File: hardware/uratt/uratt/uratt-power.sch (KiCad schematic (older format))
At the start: 66 parts

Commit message: uRATT rough footprint assignment and placement for fitment
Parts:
- removed A?: Pololu_Breakout_A4988, Module:Pololu_Breakout-16_15.2x20.3mm, symbol Driver_Motor:Pololu_Breakout_A4988
- removed C?: 47uF, symbol Device:CP1_Small
- removed C? (x2): 0.1uF, symbol Device:C_Small
- removed J?: Conn_01x04, symbol Connector_Generic:Conn_01x04
- removed R? (x3): 0, symbol Device:R_Small_US
- C17, C20, C23, C32: renamed from C?; footprint (none) -> Capacitor_SMD:C_0805_2012Metric
- C18, C19, C21, C22, C24, C25, C26, C27, C29, C31: renamed from C?; footprint (none) -> Capacitor_SMD:C_0603_1608Metric
- C28: renamed from C?; footprint (none) -> Capacitor_SMD:CP_Elec_5x3
- D11, D7, D8, D9: renamed from D?; footprint (none) -> LED_SMD:LED_0603_1608Metric_Pad1.05x0.95mm_HandSolder
- J6, J7, J8: renamed from J?; footprint (none) -> Connector_JST:JST_PH_B2B-PH-K_1x02_P2.00mm_Vertical
- L1: renamed from L?; footprint (none) -> Inductor_SMD:L_12x12mm_H4.5mm
- R28, R29, R30, R31, R32, R33, R34, R35, R36, R37, R38, R39, R40, R41, R42, R43, R44, R45, R46, R47, R48, R49: renamed from R?; footprint (none) -> Resistor_SMD:R_0603_1608Metric
- TP1, TP2, TP3, TP4, TP5, TP6: renamed from TP?; footprint (none) -> TestPoint:TestPoint_Pad_1.5x1.5mm
- U5: renamed from U?; footprint (none) -> Package_SO:TSSOP-8_4.4x3mm_P0.65mm
- U6: renamed from U?; footprint (none) -> Package_SO:TSSOP-16-1EP_4.4x5mm_P0.65mm
- gave numbers to parts that had none: 5
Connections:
- wire segments 250 -> 211
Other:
- note removed: "STEPPER MOTOR\nDRIVER (OPTIONAL)"

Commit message: WIP routing
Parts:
- added H1, H2, H3, H4: MountingHole, MountingHole:MountingHole_2.7mm_M2.5, symbol Mechanical:MountingHole
- C28: footprint Capacitor_SMD:CP_Elec_5x3 -> Capacitor_Tantalum_SMD:CP_EIA-6032-20_AVX-F
- GT1: renamed from R43; footprint Resistor_SMD:R_0603_1608Metric -> uratt:GND_TIE
- TP1, TP2, TP3, TP4, TP5, TP6: footprint TestPoint:TestPoint_Pad_1.5x1.5mm -> TestPoint:TestPoint_Pad_D1.0mm
- U6: footprint Package_SO:TSSOP-16-1EP_4.4x5mm_P0.65mm -> uratt:PWP0016C
- renumbered C31 to C30, C32 to C31, R28 to JP1, R29 to JP2, R30 to JP3, R31 to JP4, R32 to R26, R33 to R27, R34 to R28, R35 to R29, R36 to R30, R37 to R31, R38 to R32, R39 to R33, R40 to R34, R41 to R35, R42 to R36, R44 to R37, R45 to R38, R46 to R39, R47 to R40, R48 to R41, R49 to R42

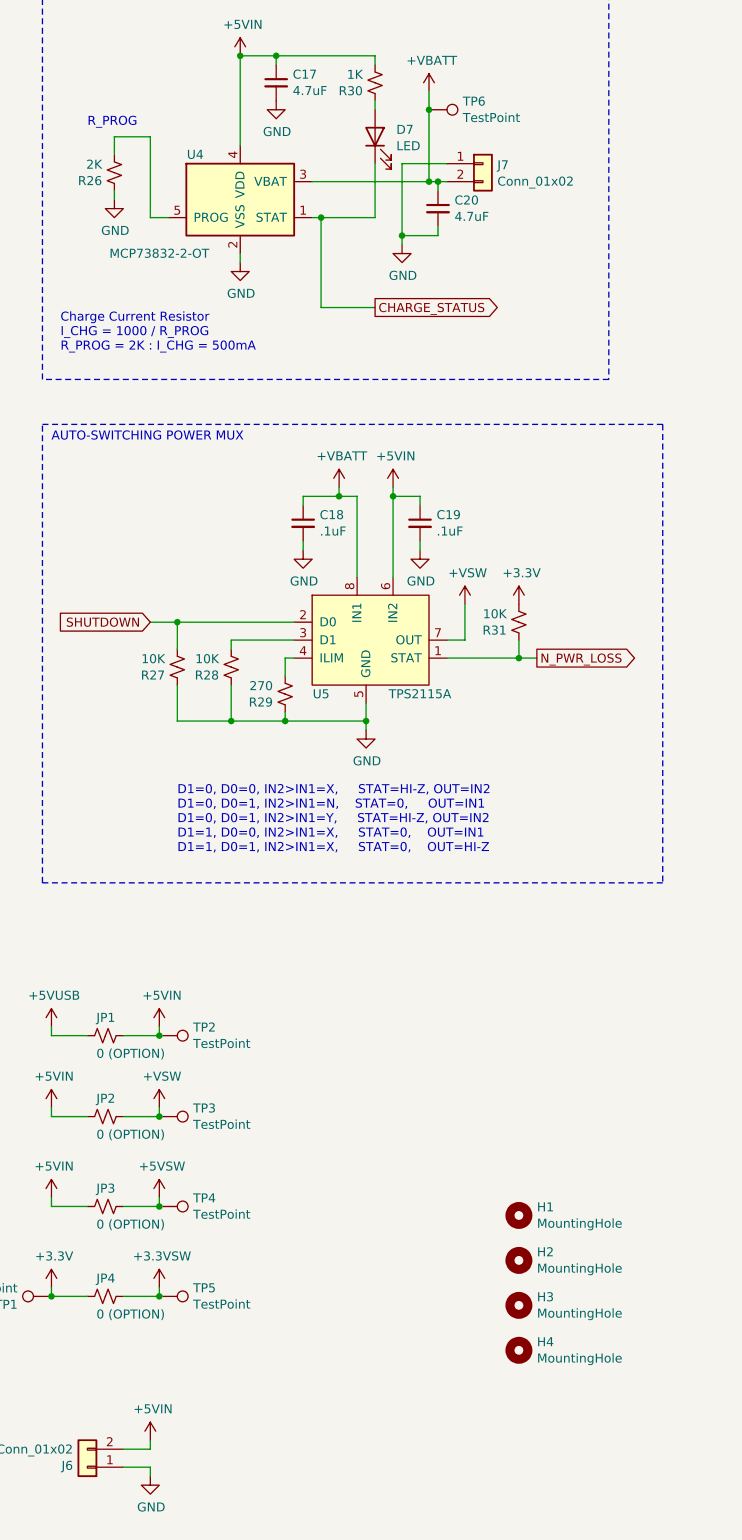
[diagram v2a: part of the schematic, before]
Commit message: fully routed, DRC'd, outlined w/breakaways, pending final review
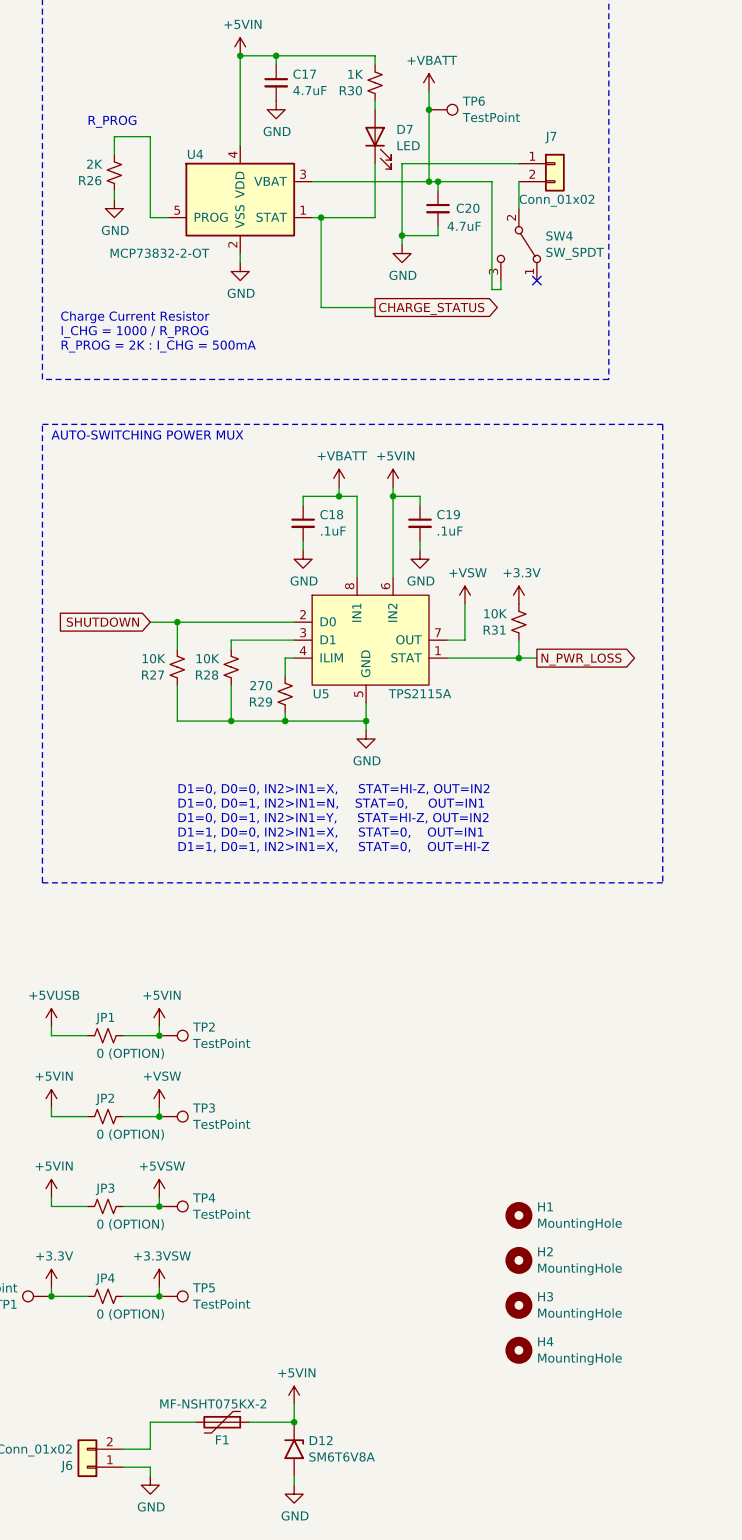
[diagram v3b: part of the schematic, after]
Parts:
- added D12: SM6T6V8A, Diode_SMD:D_SMB, symbol Diode:SM6T6V8A
- added F1: MF-NSHT075KX-2, Fuse:Fuse_1206_3216Metric, symbol Device:Polyfuse
- added SW4: SW_SPDT, uratt:EAO-SPDT, symbol Switch:SW_SPDT
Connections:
- net +5VIN: now also D12.1 (A1), F1.1; no longer J6.2 (Pin_2)
- net +VBATT: now also SW4.3 (C); no longer J7.2 (Pin_2)
- net GND: now also D12.2 (A2)
- new net: J7.2 (Pin_2), SW4.2 (B)
- new net: F1.2, J6.2 (Pin_2)
- no-connect marks 0 -> 1
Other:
- moved on the sheet: J7
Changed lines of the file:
@@
 	3900 2800 3900 2850
 Wire Wire Line
-	3900 2550 3950 2550
+	3900 2550 4200 2550
 Connection ~ 3900 2550
 Wire Wire Line
@@
 AR Path="/62033DE7" Ref="C?"  Part="1"
 AR Path="/61FC99B5/62033DE7" Ref="C20"  Part="1"
-F 0 "C20" H 3992 2746 50  0000 L CNN
-F 1 "4.7uF" H 3992 2655 50  0000 L CNN
+F 0 "C20" H 4000 2700 50  0000 L CNN
+F 1 "4.7uF" H 3950 2600 50  0000 L CNN
 F 2 "Capacitor_SMD:C_0805_2012Metric" H 3900 2700 50  0001 C CNN
 F 3 "~" H 3900 2700 50  0001 C CNN
@@
 	3700 2450 3700 2850
 Wire Wire Line
-	3950 2450 3700 2450
+	4350 2450 3700 2450
 Wire Wire Line
 	3200 2550 3850 2550
@@
 L Connector_Generic:Conn_01x02 J?
 U 1 1 62033DD8
-P 4150 2450
+P 4550 2450
 AR Path="/62033DD8" Ref="J?"  Part="1"
 AR Path="/61FC99B5/62033DD8" Ref="J7"  Part="1"
-F 0 "J7" H 4230 2442 50  0000 L CNN
-F 1 "Conn_01x02" H 4230 2351 50  0000 L CNN
-F 2 "Connector_JST:JST_PH_B2B-PH-K_1x02_P2.00mm_Vertical" H 4150 2450 50  0001 C CNN
-F 3 "~" H 4150 2450 50  0001 C CNN
-	1    4150 2450
+F 0 "J7" H 4500 2600 50  0000 L CNN
+F 1 "Conn_01x02" H 4350 2250 50  0000 L CNN
+F 2 "Connector_JST:JST_PH_B2B-PH-K_1x02_P2.00mm_Vertical" H 4550 2450 50  0001 C CNN
+F 3 "~" H 4550 2450 50  0001 C CNN
+	1    4550 2450
 	1    0    0    -1
 $EndComp
@@
 L uratt:+5VIN #PWR?
 U 1 1 6331D79A
-P 2300 9550
+P 3100 9350
 AR Path="/6331D79A" Ref="#PWR?"  Part="1"
 AR Path="/61FC99B5/6331D79A" Ref="#PWR045"  Part="1"
-F 0 "#PWR045" H 2300 9400 50  0001 C CNN
-F 1 "+5VIN" H 2315 9723 50  0000 C CNN
-F 2 "" H 2300 9550 50  0001 C CNN
-F 3 "" H 2300 9550 50  0001 C CNN
-	1    2300 9550
+F 0 "#PWR045" H 3100 9200 50  0001 C CNN
+F 1 "+5VIN" H 3115 9523 50  0000 C CNN
+F 2 "" H 3100 9350 50  0001 C CNN
+F 3 "" H 3100 9350 50  0001 C CNN
+	1    3100 9350
 	1    0    0    -1
 $EndComp
 Wire Wire Line
 	2150 9600 2300 9600
-Wire Wire Line
-	2300 9600 2300 9550
 Wire Wire Line
 	2150 7750 2350 7750
@@
 	1    0    0    -1
 $EndComp
+$Comp
+L Switch:SW_SPDT SW4
+U 1 1 5FFC2F18
+P 4350 2900
+F 0 "SW4" V 4304 3048 50  0000 L CNN
+F 1 "SW_SPDT" V 4395 3048 50  0000 L CNN
+F 2 "uratt:EAO-SPDT" H 4350 2900 50  0001 C CNN
+F 3 "~" H 4350 2900 50  0001 C CNN
+	1    4350 2900
+	0    1    1    0
+$EndComp
+Wire Wire Line
+	4350 2700 4350 2550
+Wire Wire Line
+	4250 3100 4250 3150
+Wire Wire Line
+	4250 3150 4200 3150
+Wire Wire Line
+	4200 3150 4200 2550
+NoConn ~ 4450 3100
+$Comp
+L Device:Polyfuse F1
+U 1 1 6003A919
+P 2700 9450
+F 0 "F1" V 2800 9450 50  0000 C CNN
+F 1 "MF-NSHT075KX-2" V 2600 9400 50  0000 C CNN
+F 2 "Fuse:Fuse_1206_3216Metric" H 2750 9250 50  0001 L CNN
+F 3 "~" H 2700 9450 50  0001 C CNN
+	1    2700 9450
+	0    1    1    0
+$EndComp
+Wire Wire Line
+	2300 9450 2550 9450
+Wire Wire Line
+	2300 9450 2300 9600
+Wire Wire Line
+	2850 9450 3100 9450
+Wire Wire Line
+	3100 9450 3100 9350
+$Comp
+L Diode:SM6T6V8A D12
+U 1 1 6005C353
+P 3100 9600
+F 0 "D12" V 3054 9680 50  0000 L CNN
+F 1 "SM6T6V8A" V 3145 9680 50  0000 L CNN
+F 2 "Diode_SMD:D_SMB" H 3100 9400 50  0001 C CNN
+F 3 "https://www.st.com/resource/en/datasheet/sm6t.pdf" H 3050 9600 50  0001 C CNN
+	1    3100 9600
+	0    1    1    0
+$EndComp
+Connection ~ 3100 9450
+$Comp
+L power:GND #PWR?
+U 1 1 6005EB2D
+P 3100 9800
+AR Path="/6005EB2D" Ref="#PWR?"  Part="1"
+AR Path="/61FC99B5/6005EB2D" Ref="#PWR09"  Part="1"
+F 0 "#PWR09" H 3100 9550 50  0001 C CNN
+F 1 "GND" H 3105 9627 50  0000 C CNN
+F 2 "" H 3100 9800 50  0001 C CNN
+F 3 "" H 3100 9800 50  0001 C CNN
+	1    3100 9800
+	1    0    0    -1
+$EndComp
+Wire Wire Line
+	3100 9750 3100 9800
 $EndSCHEMATC

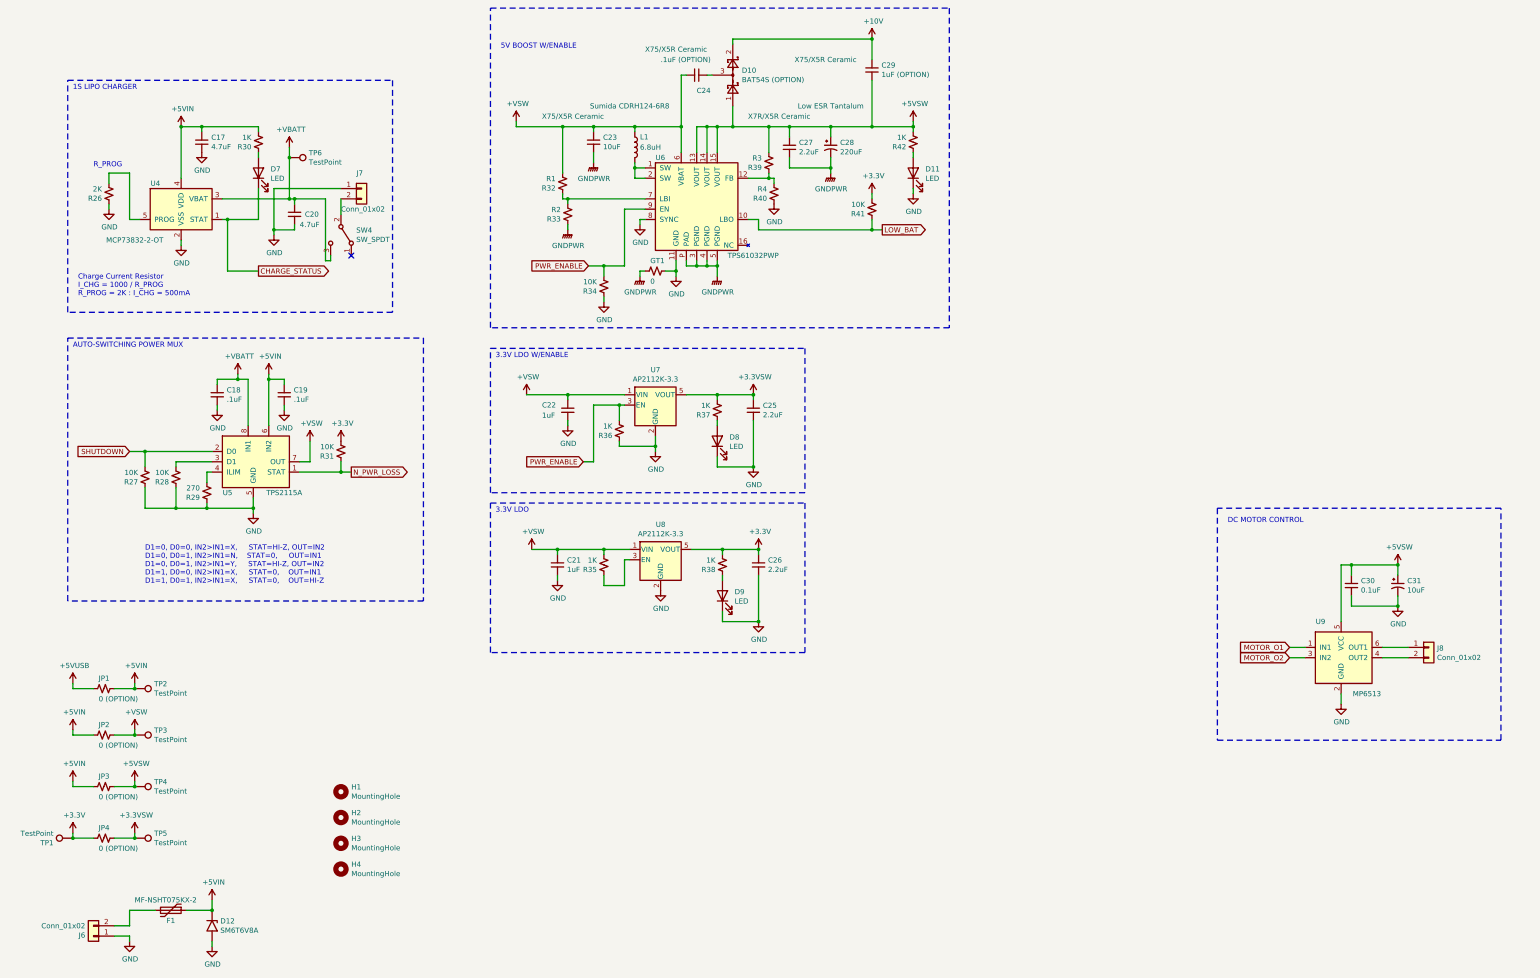
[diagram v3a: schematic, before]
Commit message: add wire passthru slot, move & finalize flat flex, bigger fp button, 10V option for motor, exp connector now Grove with I2C option
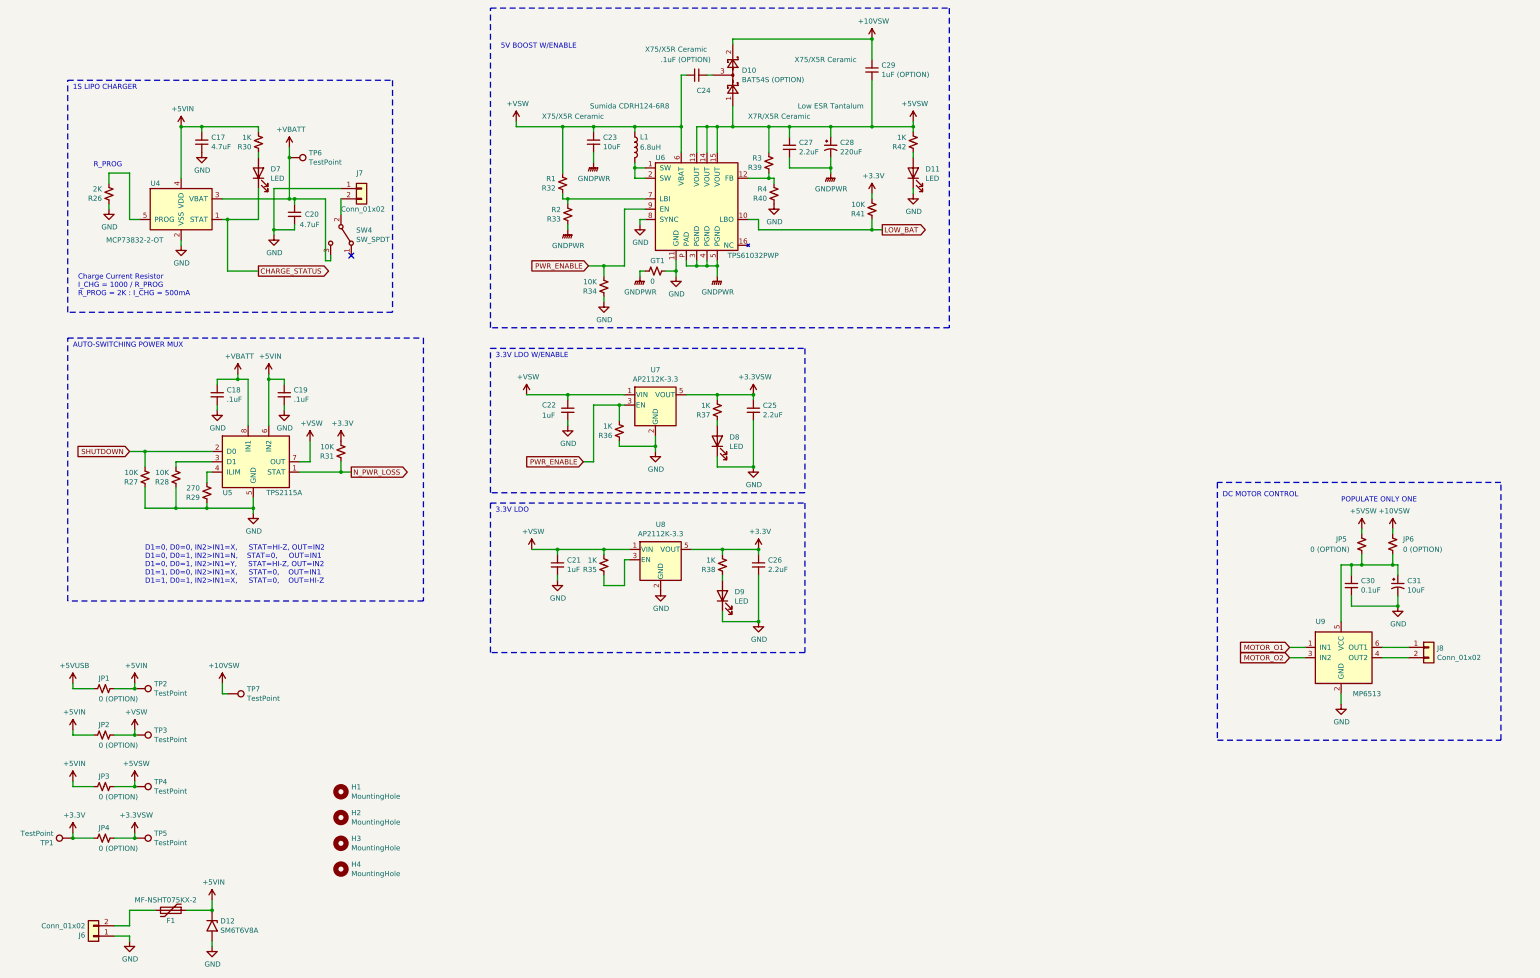
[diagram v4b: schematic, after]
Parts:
- added JP5, JP6: 0 (OPTION), Resistor_SMD:R_0603_1608Metric, symbol Device:R_Small_US
- added TP7: TestPoint, TestPoint:TestPoint_Pad_D1.0mm, symbol Connector:TestPoint
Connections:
- net +5VSW: now also JP5.1; no longer C30.1, C31.1, U9.5 (VCC)
- net +10V renamed +10VSW
- net +10VSW: now also JP6.1, TP7.1
- new net: C30.1, C31.1, JP5.2, JP6.2, U9.5 (VCC)
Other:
- note added: "POPULATE ONLY ONE"
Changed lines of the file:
@@
 Wire Wire Line
 	8150 1050 8150 1000
-Wire Wire Line
-	8150 1000 9500 1000
-$Comp
-L power:+10V #PWR083
-U 1 1 636AB9CA
-P 9500 1000
-F 0 "#PWR083" H 9500 850 50  0001 C CNN
-F 1 "+10V" H 9515 1173 50  0000 C CNN
-F 2 "" H 9500 1000 50  0001 C CNN
-F 3 "" H 9500 1000 50  0001 C CNN
-	1    9500 1000
-	1    0    0    -1
-$EndComp
 $Comp
 L Device:C_Small C?
@@
 Wire Wire Line
 	9500 1200 9500 1000
-Connection ~ 9500 1000
 Wire Wire Line
 	9500 1400 9500 1850
@@
 	13550 7000 13700 7000
 Wire Notes Line
-	12850 5550 12850 7800
+	12850 5300 12850 7800
 Wire Notes Line
 	12850 7800 15600 7800
 Wire Notes Line
-	15600 7800 15600 5550
+	15600 7800 15600 5300
 Wire Notes Line
-	15600 5550 12850 5550
-Text Notes 12950 5700 0    50   ~ 0
+	15600 5300 12850 5300
+Text Notes 12900 5450 0    50   ~ 0
 DC MOTOR CONTROL
 $Comp
 L uratt:+5VSW #PWR?
 U 1 1 63772DB6
-P 14600 6100
+P 14250 5750
 AR Path="/63772DB6" Ref="#PWR?"  Part="1"
 AR Path="/61FC99B5/63772DB6" Ref="#PWR088"  Part="1"
-F 0 "#PWR088" H 14600 5950 50  0001 C CNN
-F 1 "+5VSW" H 14615 6273 50  0000 C CNN
-F 2 "" H 14600 6100 50  0001 C CNN
-F 3 "" H 14600 6100 50  0001 C CNN
-	1    14600 6100
-	1    0    0    -1
-$EndComp
-Connection ~ 14600 6100
-Wire Wire Line
-	14150 6100 14600 6100
+F 0 "#PWR088" H 14250 5600 50  0001 C CNN
+F 1 "+5VSW" H 14265 5923 50  0000 C CNN
+F 2 "" H 14250 5750 50  0001 C CNN
+F 3 "" H 14250 5750 50  0001 C CNN
+	1    14250 5750
+	1    0    0    -1
+$EndComp
+Wire Wire Line
+	14150 6100 14250 6100
 Text GLabel 13550 6900 0    50   Input ~ 0
 MOTOR_O1
@@
 Wire Wire Line
 	3100 9750 3100 9800
+$Comp
+L Connector:TestPoint TP7
+U 1 1 5FEA27C6
+P 3250 7350
+F 0 "TP7" V 3204 7538 50  0000 L CNN
+F 1 "TestPoint" V 3295 7538 50  0000 L CNN
+F 2 "TestPoint:TestPoint_Pad_D1.0mm" H 3450 7350 50  0001 C CNN
+F 3 "~" H 3450 7350 50  0001 C CNN
+	1    3250 7350
+	0    1    1    0
+$EndComp
+Wire Wire Line
+	3250 7350 3200 7350
+$Comp
+L uratt:+10VSW #PWR010
+U 1 1 5FECDA05
+P 3200 7250
+F 0 "#PWR010" H 3200 7100 50  0001 C CNN
+F 1 "+10VSW" H 3215 7423 50  0000 C CNN
+F 2 "" H 3200 7250 50  0001 C CNN
+F 3 "" H 3200 7250 50  0001 C CNN
+	1    3200 7250
+	1    0    0    -1
+$EndComp
+Wire Wire Line
+	3200 7350 3200 7250
+$Comp
+L uratt:+10VSW #PWR036
+U 1 1 5FEEB21B
+P 9500 1000
+F 0 "#PWR036" H 9500 850 50  0001 C CNN
+F 1 "+10VSW" H 9515 1173 50  0000 C CNN
+F 2 "" H 9500 1000 50  0001 C CNN
+F 3 "" H 9500 1000 50  0001 C CNN
+	1    9500 1000
+	1    0    0    -1
+$EndComp
+Connection ~ 9500 1000
+Wire Wire Line
+	8150 1000 9500 1000
+$Comp
+L Device:R_Small_US JP?
+U 1 1 5FF0920D
+P 14250 5900
+AR Path="/5FF0920D" Ref="JP?"  Part="1"
+AR Path="/61FC99B5/5FF0920D" Ref="JP5"  Part="1"
+F 0 "JP5" H 14000 5950 50  0000 L CNN
+F 1 "0 (OPTION)" H 13750 5850 50  0000 L CNN
+F 2 "Resistor_SMD:R_0603_1608Metric" H 14250 5900 50  0001 C CNN
+F 3 "~" H 14250 5900 50  0001 C CNN
+	1    14250 5900
+	1    0    0    -1
+$EndComp
+$Comp
+L uratt:+10VSW #PWR083
+U 1 1 5FF5DD11
+P 14550 5750
+F 0 "#PWR083" H 14550 5600 50  0001 C CNN
+F 1 "+10VSW" H 14565 5923 50  0000 C CNN
+F 2 "" H 14550 5750 50  0001 C CNN
+F 3 "" H 14550 5750 50  0001 C CNN
+	1    14550 5750
+	1    0    0    -1
+$EndComp
+$Comp
+L Device:R_Small_US JP?
+U 1 1 5FF6BD30
+P 14550 5900
+AR Path="/5FF6BD30" Ref="JP?"  Part="1"
+AR Path="/61FC99B5/5FF6BD30" Ref="JP6"  Part="1"
+F 0 "JP6" H 14650 5950 50  0000 L CNN
+F 1 "0 (OPTION)" H 14650 5850 50  0000 L CNN
+F 2 "Resistor_SMD:R_0603_1608Metric" H 14550 5900 50  0001 C CNN
+F 3 "~" H 14550 5900 50  0001 C CNN
+	1    14550 5900
+	1    0    0    -1
+$EndComp
+Wire Wire Line
+	14250 5750 14250 5800
+Wire Wire Line
+	14550 5750 14550 5800
+Wire Wire Line
+	14250 6000 14250 6100
+Connection ~ 14250 6100
+Wire Wire Line
+	14250 6100 14550 6100
+Wire Wire Line
+	14550 6000 14550 6100
+Connection ~ 14550 6100
+Wire Wire Line
+	14550 6100 14600 6100
+Text Notes 14050 5500 0    50   ~ 0
+POPULATE ONLY ONE
 $EndSCHEMATC
